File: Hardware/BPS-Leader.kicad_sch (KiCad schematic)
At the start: 27 parts, among them J17 Conn_01x04, J21 SFH11-PBPC-D05-ST-BK, J5 Conn_02x06_Counter_Clockwise, J6 PeripheralCAN, J7 PeripheralCAN, Q11 PMV213SN,215, U12 SHT4x

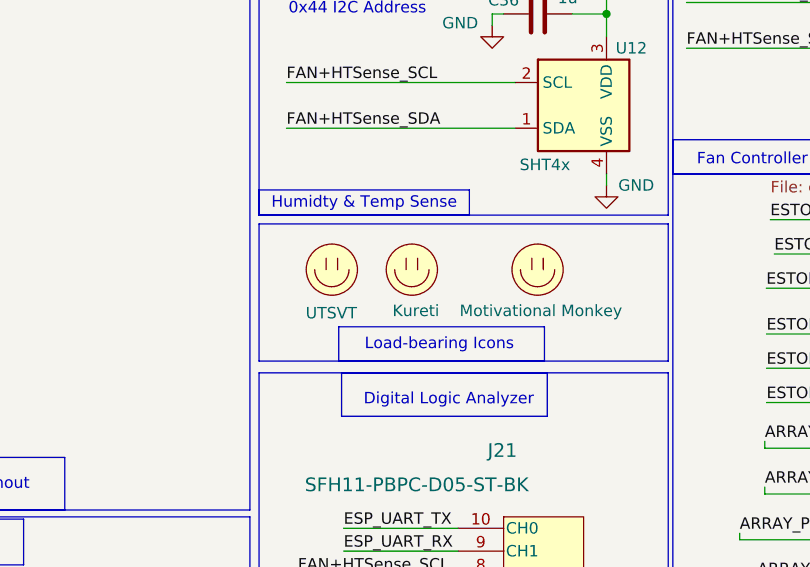
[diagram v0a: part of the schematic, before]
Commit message: all 3d models added, minor fixes
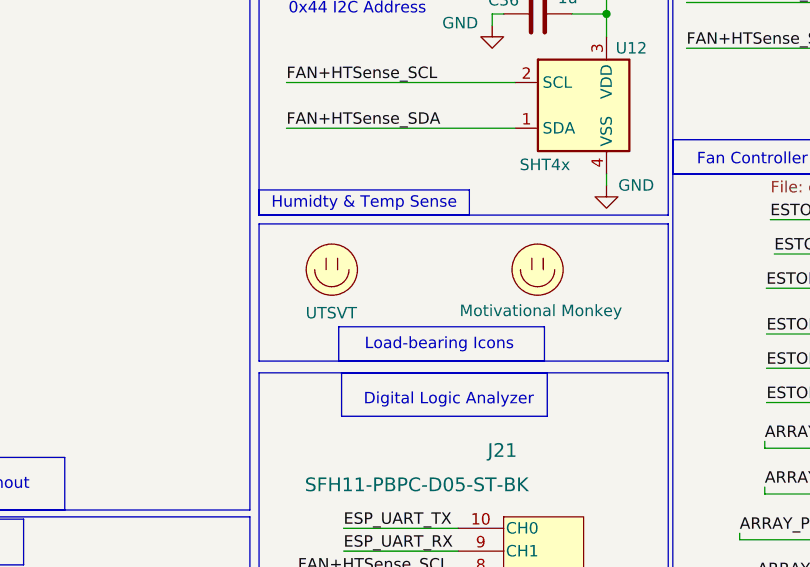
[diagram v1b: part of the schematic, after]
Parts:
- removed LOGO2: Kureti, UTSVT_Logos:Hallock_Image_Tiny, symbol UTSVT_Misc:Logo_Placeholder
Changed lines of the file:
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@@
-	)
-	(symbol
-		(lib_id "UTSVT_Misc:Logo_Placeholder")
-		(at 193.0005 102.0713 0)
-		(mirror y)
-		(unit 1)
-		(exclude_from_sim no)
-		(in_bom yes)
-		(on_board yes)
-		(dnp no)
-		(property "Reference" "LOGO2"
-			(at 193.0005 98.2613 0)
-			(effects
-				(font
-					(size 1.27 1.27)
-				)
-				(hide yes)
-			)
-		)
-		(property "Value" "Kureti"
-			(at 196.0485 106.6433 0)
-			(effects
-				(font
-					(size 1.27 1.27)
-				)
-				(justify left)
-			)
-		)
-		(property "Footprint" "UTSVT_Logos:Hallock_Image_Tiny"
-			(at 193.0005 100.1663 0)
-			(effects
-				(font
-					(size 1.27 1.27)
-				)
-				(hide yes)
-			)
-		)
-		(property "Datasheet" ""
-			(at 193.0005 100.1663 0)
-			(effects
-				(font
-					(size 1.27 1.27)
-				)
-				(hide yes)
-			)
-		)
-		(property "Description" "Graph footprint placeholder"
-			(at 193.0005 102.0713 0)
-			(effects
-				(font
-					(size 1.27 1.27)
-				)
-				(hide yes)
-			)
-		)
-		(property "PN" ""
-			(at 193.0005 102.0713 0)
-			(effects
-				(font
-					(size 1.27 1.27)
-				)
-				(hide yes)
-			)
-		)
-		(property "p/n" ""
-			(at 193.0005 102.0713 0)
-			(effects
-				(font
-					(size 1.27 1.27)
-				)
-				(hide yes)
-			)
-		)
-		(property "Manufactuerer" ""
-			(at 193.0005 102.0713 0)
-			(effects
-				(font
-					(size 1.27 1.27)
-				)
-				(hide yes)
-			)
-		)
-		(instances
-			(project "BPS-Leader"
-				(path "/fb37da34-e420-4994-8cc1-079e8c0fa48e"
-					(reference "LOGO2")
-					(unit 1)
-				)
-			)
-		)
 	)
 	(symbol

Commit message: small fixes
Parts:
- C36: P/N (none) -> C0805C105K5PACTU
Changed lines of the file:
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@@
+			)
+		)
+		(property "P/N" "C0805C105K5PACTU"
+			(at 207.01 73.66 90)
+			(effects
+				(font
+					(size 1.27 1.27)
+				)
+				(hide yes)
 			)
 		)

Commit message: added BOM
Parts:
- C36: Manufactuerer (none) -> TAIYO YUDEN; P/N C0805C105K5PACTU -> MLASU168SB5105KTNA01
- F3: Manufactuerer (none) -> Keystone Electronics; P/N (none) -> 3568
- J1, LOGO1, LOGO3, TP2, TP29, TP3, TP30, TP31, TP32, TP33, TP49, TP50: now left out of the parts list
- J17: Manufactuerer (none) -> Molex; P/N (none) -> 105309-1204
- J21: Manufactuerer (none) -> Sullins Connector Solutions
- J5: Manufactuerer (none) -> Molex; P/N (none) -> 105310-1112
- J6, J7: Manufactuerer (none) -> Molex
- Q11: Manufactuerer (none) -> Nexperia; P/N (none) -> PMV213SN,215
- R66: Manufactuerer (none) -> Vishay; P/N (none) -> CRCW060310K0FKEI
- U12: Manufactuerer (none) -> Sensirion; P/N (none) -> SHT45-AD1B-R2
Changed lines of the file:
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@@
 			)
 		)
-		(property "Datasheet" "~"
+		(property "Datasheet" "https://tools.molex.com/pdm_docs/sd/1053091204_sd.pdf"
 			(at 49.53 184.15 0)
 			(effects
@@
 			)
 		)
-		(property "Manufactuerer" ""
+		(property "Manufactuerer" "Molex "
+			(at 49.53 184.15 0)
+			(effects
+				(font
+					(size 1.27 1.27)
+				)
+				(hide yes)
+			)
+		)
+		(property "P/N" "105309-1204 "
 			(at 49.53 184.15 0)
 			(effects
@@
 		(unit 2)
 		(exclude_from_sim no)
-		(in_bom yes)
+		(in_bom no)
 		(on_board yes)
 		(dnp no)
@@
 			)
 		)
-		(property "Datasheet" "https://www.mouser.com/ProductDetail/Molex/105309-1204?qs=PqFvFmEiOr6mDAWV2BJKbg%3D%3D&srsltid=AfmBOopk7YsqdMLo2_DAHKaHKt3Hg126ooPXYWv5Q2Pfx6rW7DaYZCT2"
+		(property "Datasheet" "https://tools.molex.com/pdm_docs/sd/1053091204_sd.pdf"
 			(at 182.88 48.26 0)
 			(effects
@@
 			)
 		)
-		(property "Manufactuerer" ""
+		(property "Manufactuerer" "Molex "
 			(at 177.8 55.88 0)
 			(effects
@@
 		(unit 1)
 		(exclude_from_sim no)
-		(in_bom yes)
+		(in_bom no)
 		(on_board yes)
 		(dnp no)
@@
 			)
 		)
-		(property "Datasheet" "https://www.mouser.com/ProductDetail/Molex/105309-1204?qs=PqFvFmEiOr6mDAWV2BJKbg%3D%3D&srsltid=AfmBOopk7YsqdMLo2_DAHKaHKt3Hg126ooPXYWv5Q2Pfx6rW7DaYZCT2"
+		(property "Datasheet" "https://tools.molex.com/pdm_docs/sd/1053091204_sd.pdf"
 			(at 134.62 48.26 0)
 			(effects
@@
 			)
 		)
-		(property "Manufactuerer" ""
+		(property "Manufactuerer" "Molex "
 			(at 129.54 55.88 0)
 			(effects
@@
 		(unit 1)
 		(exclude_from_sim no)
-		(in_bom yes)
+		(in_bom no)
 		(on_board yes)
 		(dnp no)
@@
 		(unit 1)
 		(exclude_from_sim no)
-		(in_bom yes)
+		(in_bom no)
 		(on_board yes)
 		(dnp no)
@@
 		(unit 1)
 		(exclude_from_sim no)
-		(in_bom yes)
+		(in_bom no)
 		(on_board yes)
 		(dnp no)
@@
 			)
 		)
-		(property "Datasheet" "~"
+		(property "Datasheet" "https://tools.molex.com/pdm_docs/sd/1053101112_sd.pdf"
 			(at 184.15 29.21 0)
 			(effects
@@
 			)
 		)
-		(property "Manufactuerer" ""
+		(property "Manufactuerer" "Molex "
+			(at 184.15 29.21 0)
+			(effects
+				(font
+					(size 1.27 1.27)
+				)
+				(hide yes)
+			)
+		)
+		(property "P/N" "105310-1112 "
 			(at 184.15 29.21 0)
 			(effects
@@
 		(unit 1)
 		(exclude_from_sim no)
-		(in_bom yes)
+		(in_bom no)
 		(on_board yes)
 		(dnp no)
@@
 		(unit 1)
 		(exclude_from_sim no)
-		(in_bom yes)
+		(in_bom no)
 		(on_board yes)
 		(dnp no)
@@
 		(unit 1)
 		(exclude_from_sim no)
-		(in_bom yes)
+		(in_bom no)
 		(on_board yes)
 		(dnp no)
@@
 			)
 		)
-		(property "Datasheet" "https://sensirion.com/media/documents/33FD6951/624C4357/Datasheet_SHT4x.pdf"
+		(property "Datasheet" "https://www.mouser.com/datasheet/3/1278/1/HT_DS_Datasheet_SHT4x_5.pdf"
 			(at 215.9 92.71 0)
 			(effects
@@
 			)
 		)
-		(property "Manufactuerer" ""
+		(property "Manufactuerer" "Sensirion "
+			(at 212.09 83.82 0)
+			(effects
+				(font
+					(size 1.27 1.27)
+				)
+				(hide yes)
+			)
+		)
+		(property "P/N" "SHT45-AD1B-R2 "
 			(at 212.09 83.82 0)
 			(effects
@@
 			)
 		)
-		(property "Datasheet" "~"
+		(property "Datasheet" "https://www.mouser.com/datasheet/3/201/1/3568.PDF"
 			(at 172.72 26.67 0)
 			(effects
@@
 			)
 		)
-		(property "Manufactuerer" ""
+		(property "Manufactuerer" "Keystone Electronics "
 			(at 172.72 26.67 0)
 			(effects
@@
 			)
 		)
+		(property "P/N" "3568"
+			(at 172.72 26.67 90)
+			(effects
+				(font
+					(size 1.27 1.27)
+				)
+				(hide yes)
+			)
+		)
 		(pin "2"
 		)
@@
 		(unit 1)
 		(exclude_from_sim no)
-		(in_bom yes)
+		(in_bom no)
 		(on_board yes)
 		(dnp no)
@@
 			)
 		)
-		(property "Datasheet" "https://www.digikey.com/en/products/detail/sullins-connector-solutions/SFH11-PBPC-D05-ST-BK/1990087?gclsrc=aw.ds&gad_source=1&gad_campaignid=120565755&gbraid=0AAAAADrbLljEsXDDEt5svizMM4jeYrL-A&gclid=Cj0KCQjwwZDFBhCpARIsAB95qO2YCKMg2VQme3QQBBCFa3dTLVMMS-qCbMZE8KZJpYe-_Bi6ULwi-x0aAvv3EALw_wcB"
+		(property "Datasheet" "https://s3.amazonaws.com/catalogspreads-pdf/PAGE123%20.100%20SFH11%20SERIES%20FEMALE%20HDR%20ST%20RA.pdf"
 			(at 206.502 123.19 0)
 			(effects
@@
 			)
 		)
-		(property "Manufactuerer" ""
+		(property "Manufactuerer" "Sullins Connector Solutions"
 			(at 198.12 132.08 0)
 			(effects
@@
 		(unit 1)
 		(exclude_from_sim no)
-		(in_bom yes)
+		(in_bom no)
 		(on_board yes)
 		(dnp no)
@@
 			)
 		)
-		(property "Datasheet" "~"
+		(property "Datasheet" "https://www.vishay.com/docs/20035/dcrcwe3.pdf"
 			(at 148.59 21.59 0)
 			(effects
@@
 			)
 		)
-		(property "Manufactuerer" ""
+		(property "Manufactuerer" "Vishay "
+			(at 148.59 21.59 90)
+			(effects
+				(font
+					(size 1.27 1.27)
+				)
+				(hide yes)
+			)
+		)
+		(property "P/N" "CRCW060310K0FKEI "
 			(at 148.59 21.59 90)
 			(effects
@@
 			)
 		)
-		(property "Datasheet" "~"
+		(property "Datasheet" "https://ds.yuden.co.jp/TYCOMPAS/or/download?pn=MLAST063SCG681JFNA01&fileType=CA"
 			(at 207.01 73.66 0)
 			(effects
@@
 			)
 		)
-		(property "Manufactuerer" ""
+		(property "Manufactuerer" "TAIYO YUDEN "
 			(at 207.01 73.66 0)
 			(effects
@@
 			)
 		)
-		(property "P/N" "C0805C105K5PACTU"
+		(property "P/N" "MLASU168SB5105KTNA01"
 			(at 207.01 73.66 90)
 			(effects
@@
 		(unit 1)
 		(exclude_from_sim no)
-		(in_bom yes)
+		(in_bom no)
 		(on_board yes)
 		(dnp no)
@@
 			)
 		)
-		(property "Datasheet" "https://assets.nexperia.com/documents/data-sheet/PMV213SN.pdf"
+		(property "Datasheet" "https://www.mouser.com/ProductDetail/Nexperia/PMV213SN215?qs=LOCUfHb8d9sH6YyLGIT8fQ%3D%3D"
 			(at 147.32 33.02 0)
 			(effects
@@
 			)
 		)
-		(property "Manufactuerer" ""
+		(property "Manufactuerer" "Nexperia "
+			(at 143.51 27.94 0)
+			(effects
+				(font
+					(size 1.27 1.27)
+				)
+				(hide yes)
+			)
+		)
+		(property "P/N" "PMV213SN,215 "
 			(at 143.51 27.94 0)
 			(effects
@@
 		(unit 1)
 		(exclude_from_sim no)
-		(in_bom yes)
+		(in_bom no)
 		(on_board yes)
 		(dnp no)
@@
 		(unit 1)
 		(exclude_from_sim no)
-		(in_bom yes)
+		(in_bom no)
 		(on_board yes)
 		(dnp no)

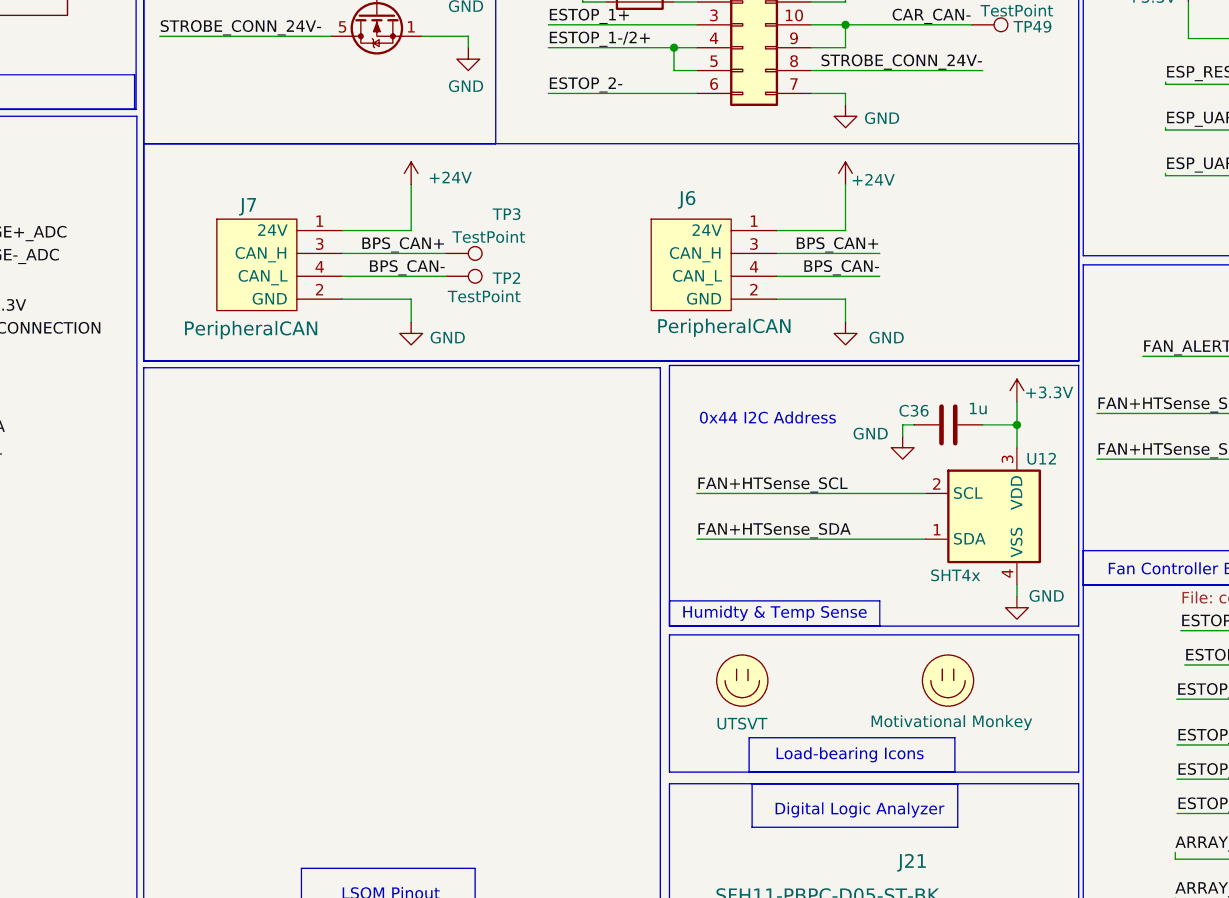
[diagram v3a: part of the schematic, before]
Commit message: Rerouted traces to distribute damage to ground plane, labled connectors, added a Charger Can port contected to CarCan Terminals, removed via constriction on main power traces (24V and 3.3V) and expanded 24V plane on RPP circuit to increase current flow, other minor silkscreen tweaks
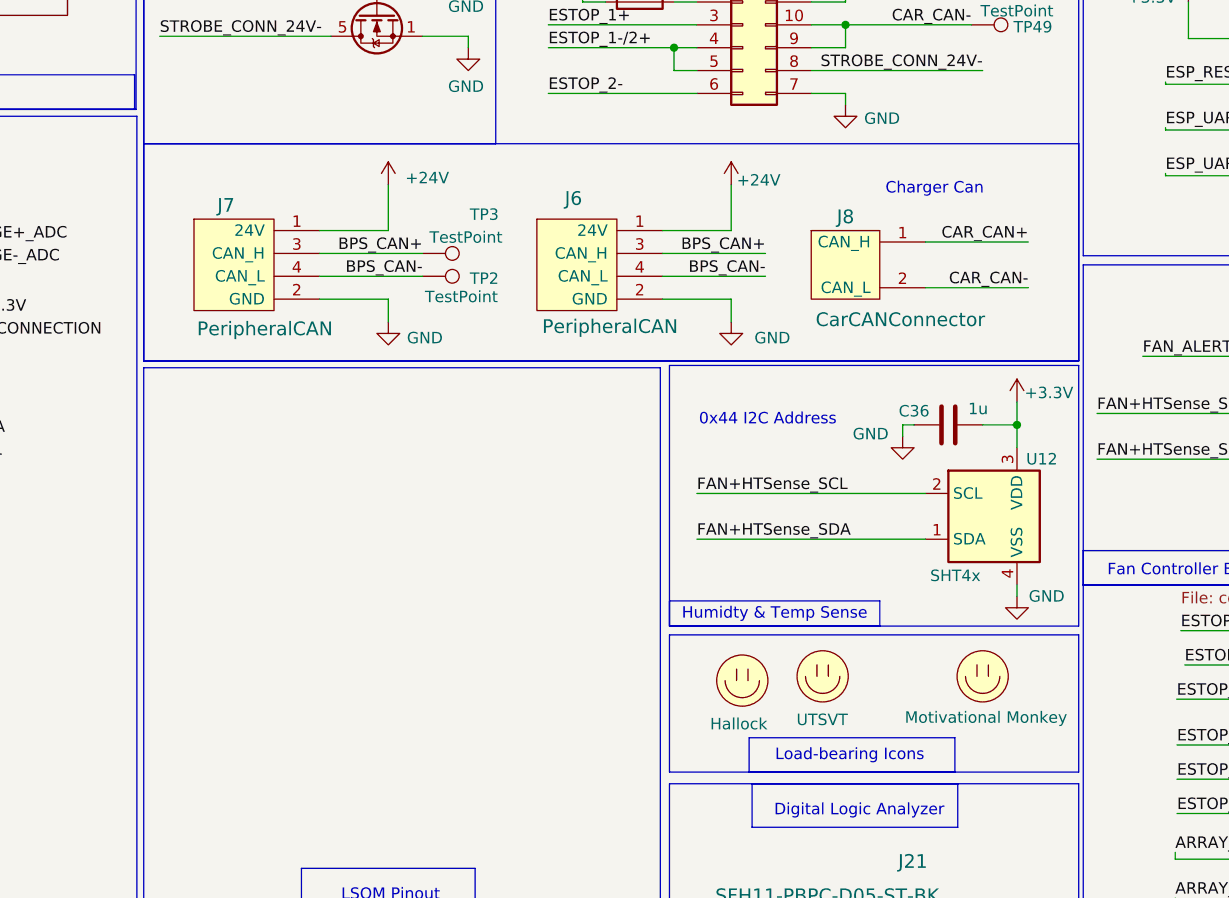
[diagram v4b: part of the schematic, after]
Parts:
- added J8: CarCANConnector, UTSVT_Connectors:Molex_Nano-Fit_105309-xx02_1x02_P2.50mm_Vertical, symbol utsvt_connectors:CarCANConnector
- added LOGO2: UTSVT, UTSVT_Logos:UTSVT_Logo_Symbol, symbol UTSVT_Misc:Logo_Placeholder
- LOGO3: value UTSVT -> Hallock
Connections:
- net CAR_CAN+: now also J8.1 (CAN_H)
- net CAR_CAN-: now also J8.2 (CAN_L)
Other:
- note added: "Charger Can"
- moved on the sheet: J6, J7, TP2, TP3

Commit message: Board GERBER genereated and BOM :)
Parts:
- removed F3: Fuse, FUSE 3568:3568, symbol Device:Fuse
- added F2: 3568, FUSE 3568:3568, symbol 3568:3568
- LOGO2: footprint UTSVT_Logos:UTSVT_Logo_Symbol -> UTSVT_Logos:LHRs_LOGO
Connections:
- net +24V: now also F2.1, F2.3
- net FAN+HTSense_SCL: now also J21.6 (CH4); no longer J21.8 (CH2)
- net FAN_1_PWM: now also J21.8 (CH2); no longer J21.6 (CH4)
- net at J5.2 (Pin_2): now also F2.2, F2.4
